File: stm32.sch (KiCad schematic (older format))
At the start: 37 parts, among them J1 USB_B_Micro, J2 Conn_02x05_Odd_Even, U1 STM32F767VITx, U5 LM2937, X1 8MHz

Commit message: Ready To Go! (#53)
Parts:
- C39: Manufacturer (none) -> AVX; VEND (none) -> MOUSER; VEND# (none) -> 581-TAJA156M010R
- D14: Manufacturer DIALIGHT -> (none); Part # 599-0281-007F -> (none); VEND MOUSER -> (none); VEND# 645-599-0281-007F -> (none)
- J1: Manufacturer (none) -> MOLEX; Part # (none) -> 105133-0031; VEND (none) -> MOUSER
- J2: VEND (none) -> MOUSER
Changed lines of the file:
@@
 F 4 "stm32f407_board" H 23450 3775 60  0001 C CNN "PageName"
 F 5 "TAJA156M010RNJ" H 0   0   50  0001 C CNN "Part #"
+F 6 "AVX" H 0   0   50  0001 C CNN "Manufacturer"
+F 7 "MOUSER" H 0   0   50  0001 C CNN "VEND"
+F 8 "581-TAJA156M010R" H 0   0   50  0001 C CNN "VEND#"
 	1    15350 2900
 	1    0    0    -1
@@
 F 3 "" H 12150 3800 60  0001 C CNN
 F 4 "stm32f407_board" H 11525 1275 60  0001 C CNN "PageName"
-F 5 "MOUSER" H -6450 -2300 50  0001 C CNN "VEND"
-F 6 "DIALIGHT" H -6450 -2300 50  0001 C CNN "Manufacturer"
-F 7 "599-0281-007F" H -6450 -2300 50  0001 C CNN "Part #"
-F 8 "645-599-0281-007F" H -6450 -2300 50  0001 C CNN "VEND#"
 	1    12150 3800
 	-1   0    0    1
@@
 F 2 "Connector_PinSocket_2.54mm:PinSocket_2x05_P2.54mm_Vertical_SMD" H 11800 6200 50  0001 C CNN
 F 3 "~" H 11800 6200 50  0001 C CNN
+F 4 "MOUSER" H 0   0   50  0001 C CNN "VEND"
 	1    11800 6200
 	1    0    0    -1
@@
 F 2 "Connector_USB:USB_Micro-B_Molex-105133-0031" H 11650 4150 50  0001 C CNN
 F 3 "~" H 11650 4150 50  0001 C CNN
+F 4 "MOLEX" H 0   0   50  0001 C CNN "Manufacturer"
+F 5 "105133-0031" H 0   0   50  0001 C CNN "Part #"
+F 6 "MOUSER" H 0   0   50  0001 C CNN "VEND"
 	1    11500 4200
 	1    0    0    -1

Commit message: 2x5 BOM and small fix
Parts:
- J2: Manufacturer (none) -> Amphenol; Part # (none) -> 95278-801B10LF; VEND# (none) -> 649-95278-801B10LF
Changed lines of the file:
@@
 F 3 "~" H 11800 6200 50  0001 C CNN
 F 4 "MOUSER" H 0   0   50  0001 C CNN "VEND"
+F 5 "Amphenol" H 0   0   50  0001 C CNN "Manufacturer"
+F 6 "95278-801B10LF" H 0   0   50  0001 C CNN "Part #"
+F 7 "649-95278-801B10LF" H 0   0   50  0001 C CNN "VEND#"
 	1    11800 6200
 	1    0    0    -1

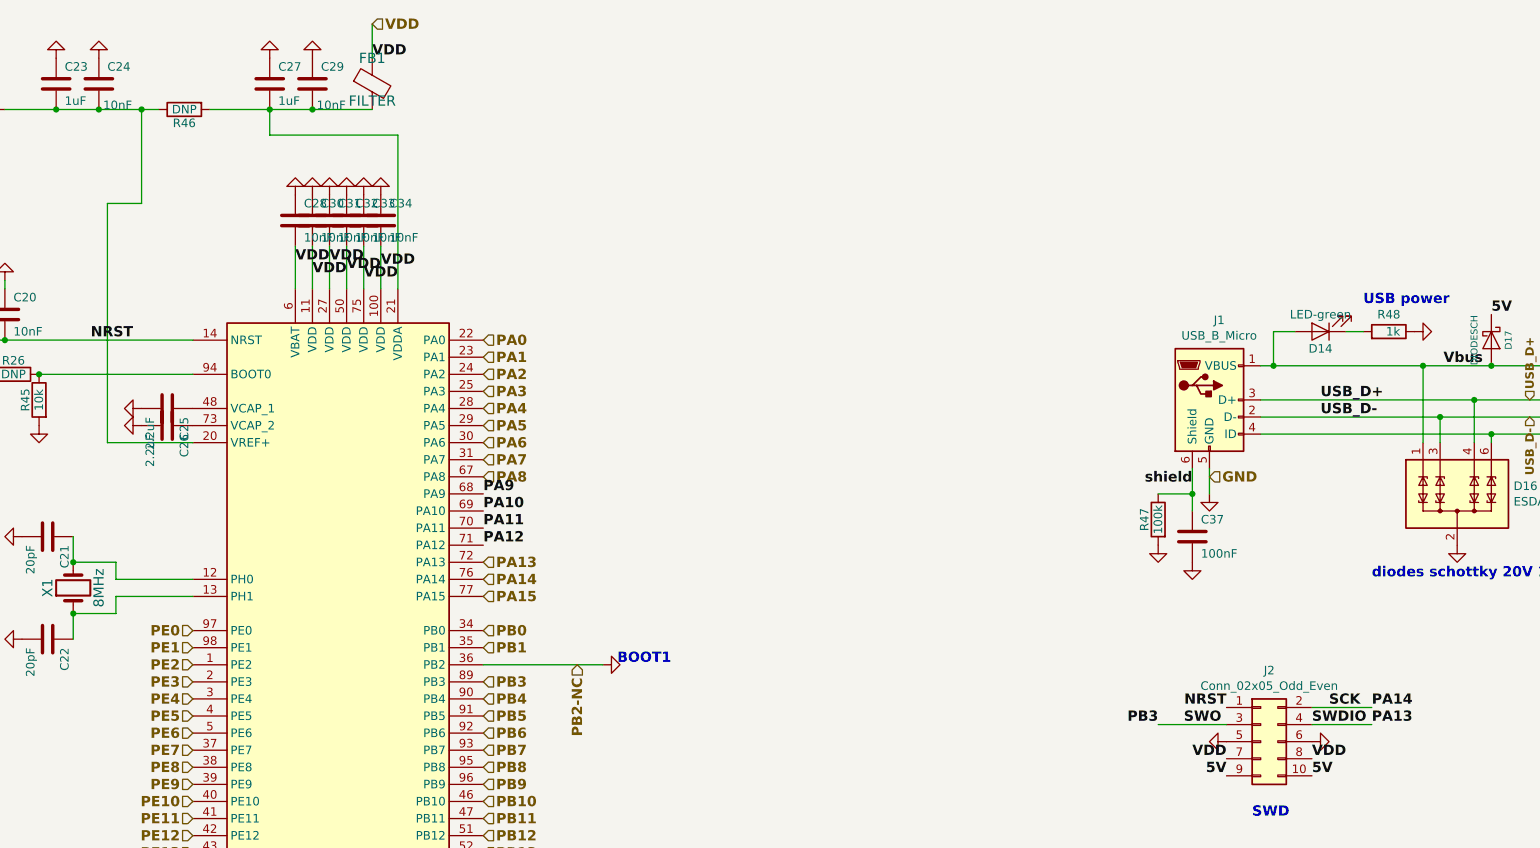
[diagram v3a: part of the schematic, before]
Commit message: from Ola and Jared (#71)
* Update

* removed fp-info-cache from git

* Gerbers

* moved connector

* Mostly Ola's e-mailed copy, plus some of my own fixes to his almost done revision. I also did some house cleaning, with boundary edges, removed most DRC and ERC errors, etc.

* added Fiducial's
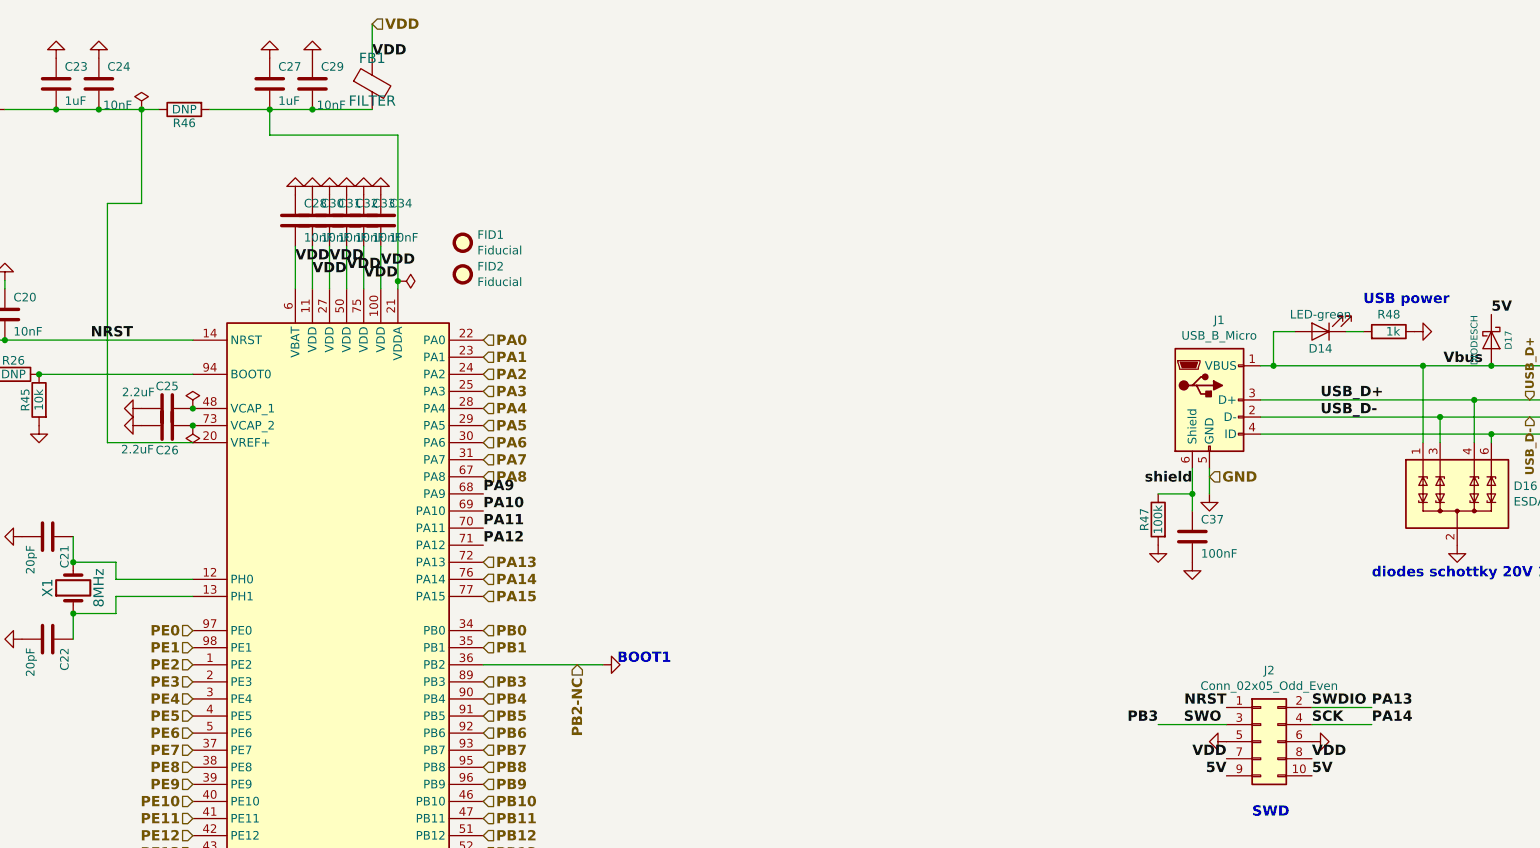
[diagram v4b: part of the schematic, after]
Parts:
- added FID1, FID2: Fiducial, Fiducial:Fiducial_0.5mm_Mask1mm, symbol Mechanical:Fiducial
- C20, C21, C22, C23, C24, C25, C26, C27, C28, C29, C30, C31, C32, C33, C34, C36, C37, C38: footprint Capacitor_SMD:C_0603_1608Metric_Pad1.05x0.95mm_HandSolder -> Capacitor_SMD:C_0603_1608Metric
- C39: footprint Capacitor_SMD:C_1206_3216Metric_Pad1.42x1.75mm_HandSolder -> Capacitor_SMD:C_1206_3216Metric
- D17: footprint Capacitor_SMD:C_0603_1608Metric_Pad1.05x0.95mm_HandSolder -> Diode_SMD:D_0603_1608Metric
- D19: footprint LED_SMD:LED_0603_1608Metric_Pad1.05x0.95mm_HandSolder -> LED_SMD:LED_0603_1608Metric
- R26, R43, R44, R45, R46, R47, R48, R50: footprint Resistor_SMD:R_0603_1608Metric_Pad1.05x0.95mm_HandSolder -> Resistor_SMD:R_0603_1608Metric
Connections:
- net PA13: now also J2.2 (Pin_2); no longer J2.4 (Pin_4)
- net PA14: now also J2.4 (Pin_4); no longer J2.2 (Pin_2)

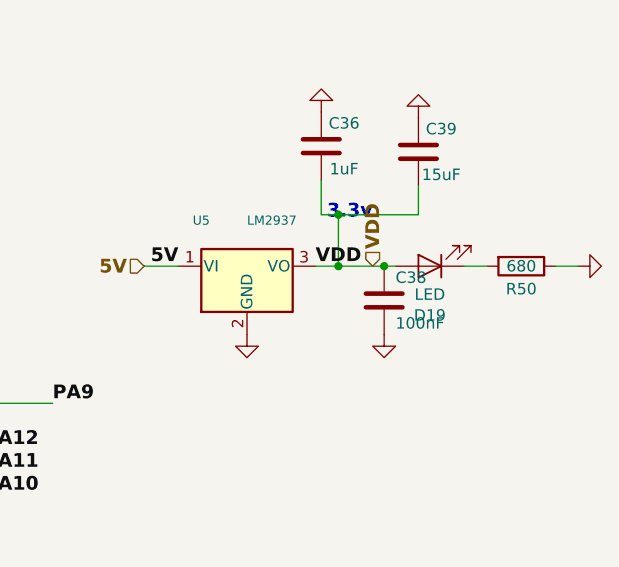
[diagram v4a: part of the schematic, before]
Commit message: Updated logo symbol and footprint, BOM is 99% entered in KC schematic now.
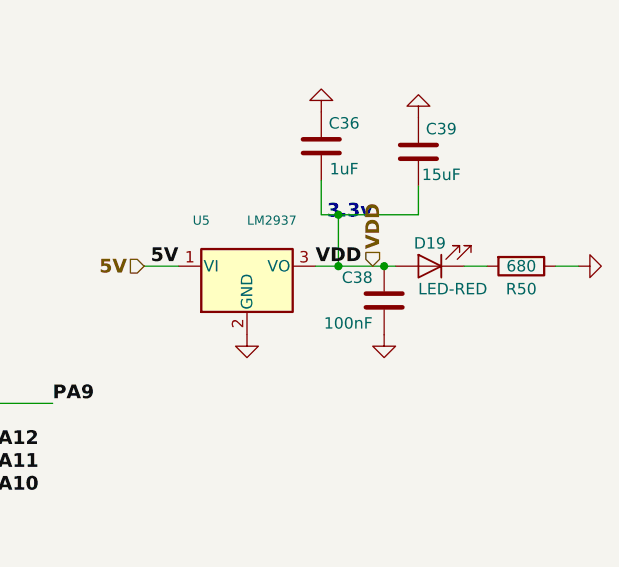
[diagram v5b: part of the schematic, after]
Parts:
- C20, C24, C28, C29, C30, C31, C32, C33, C34: Manufacturer (none) -> KEMET; Part # (none) -> C0603C103K1RACTU; VEND (none) -> DIGI; VEND# (none) -> 399-3189-1-ND
- C21, C22: Manufacturer (none) -> AVX; Part # (none) -> 06035A200FAT2A; VEND (none) -> DIGI; VEND# (none) -> 478-10299-1-ND
- C23, C27, C36: Manufacturer (none) -> Taiyo Yuden; PageName stm32f407_board -> (none); Part # (none) -> UMK107BJ105KA-T; VEND (none) -> DIGI; VEND# (none) -> 587-2400-1-ND
- C25, C26: Manufacturer (none) -> MURATA; Part # (none) -> GRM188R6YA225KA12D; VEND (none) -> DIGI; VEND# (none) -> 490-7204-1-ND
- C37, C38: Manufacturer (none) -> KEMET; Part # (none) -> C0603C104J5RACTU; VEND (none) -> DIGI; VEND# (none) -> 399-7844-1-ND
- C39: VEND MOUSER -> DIGI; VEND# 581-TAJA156M010R -> 478-1661-1-ND
- D14: Manufacturer (none) -> DiaLight; Part # (none) -> 5990281007F; VEND (none) -> DIGI; VEND# (none) -> 350-4365-1-ND
- D16: Manufacturer (none) -> ST; Part # (none) -> ESDA6V1BC6; VEND (none) -> DIGI; VEND# (none) -> 497-6635-1-ND
- D17: Manufacturer (none) -> ST; Part # ST,BAT60JFILM -> BAT60JFILM; VEND (none) -> DIGI; VEND# DIGI,497-3707-1-ND -> 497-3707-1-ND
- D19: value LED -> LED-RED; Manufacturer (none) -> Lite-On; Part # (none) -> LTST-S270KRKT; VEND (none) -> DIGI; VEND# (none) -> 160-1479-1-ND
- FB1: Manufacturer (none) -> Murata; VEND MOUSER -> DIGI; VEND# 81-BLM21P221SG -> 490-1054-1-ND
- FID1, FID2: Manufacturer (none) -> DNP; Part # (none) -> DNP; VEND (none) -> DNP; VEND# (none) -> DNP
- J1: VEND# (none) -> 538-105133-0031
- R26, R46: Manufacturer (none) -> DNP; Part # (none) -> DNP; VEND (none) -> DIGI; VEND# (none) -> DNP
- R43, R45: Manufacturer (none) -> StackPole; Part # (none) -> RMCF0603JT10K0; VEND (none) -> DIGI; VEND# (none) -> RMCF0603JT10K0CT-ND
- R44: Manufacturer (none) -> StackPole; Part # (none) -> RMCF0603ZT0R00; VEND (none) -> DIGI; VEND# (none) -> RMCF0603ZT0R00CT-ND
- R47: Manufacturer (none) -> StackPole; Part # (none) -> RMCF0603JT100K; VEND MOUSER -> DIGI; VEND# (none) -> RMCF0603JT100KCT-ND
- R48: Manufacturer (none) -> StackPole; Part # (none) -> RMCF0603JJ1K00; VEND (none) -> DIGI; VEND# (none) -> RMCF0603JJ1K00CT-ND
- R50: Manufacturer (none) -> StackPole; Part # (none) -> RMCF0603FT680R; VEND (none) -> DIGI; VEND# (none) -> RMCF0603FT680RCT-ND
- U1: Manufacturer (none) -> ST; Part # 511-STM32F767VIT6 -> STM32F767VIT6; VEND (none) -> DIGI; VEND# 511-STM32F767VIT6 -> 497-16643-ND
- U5: Manufacturer (none) -> TI; Part # 926-LM2937IMP3.3NOPB -> LM2937IMP-3.3/NOPB; VEND MOUSER -> DIGI; VEND# (none) -> LM2937IMP-3.3/NOPBCT-ND
- X1: Manufacturer (none) -> NDK; VEND MOUSER -> DIGI; VEND# 344-NX3225GD8MCRA3 -> 644-1178-1-ND

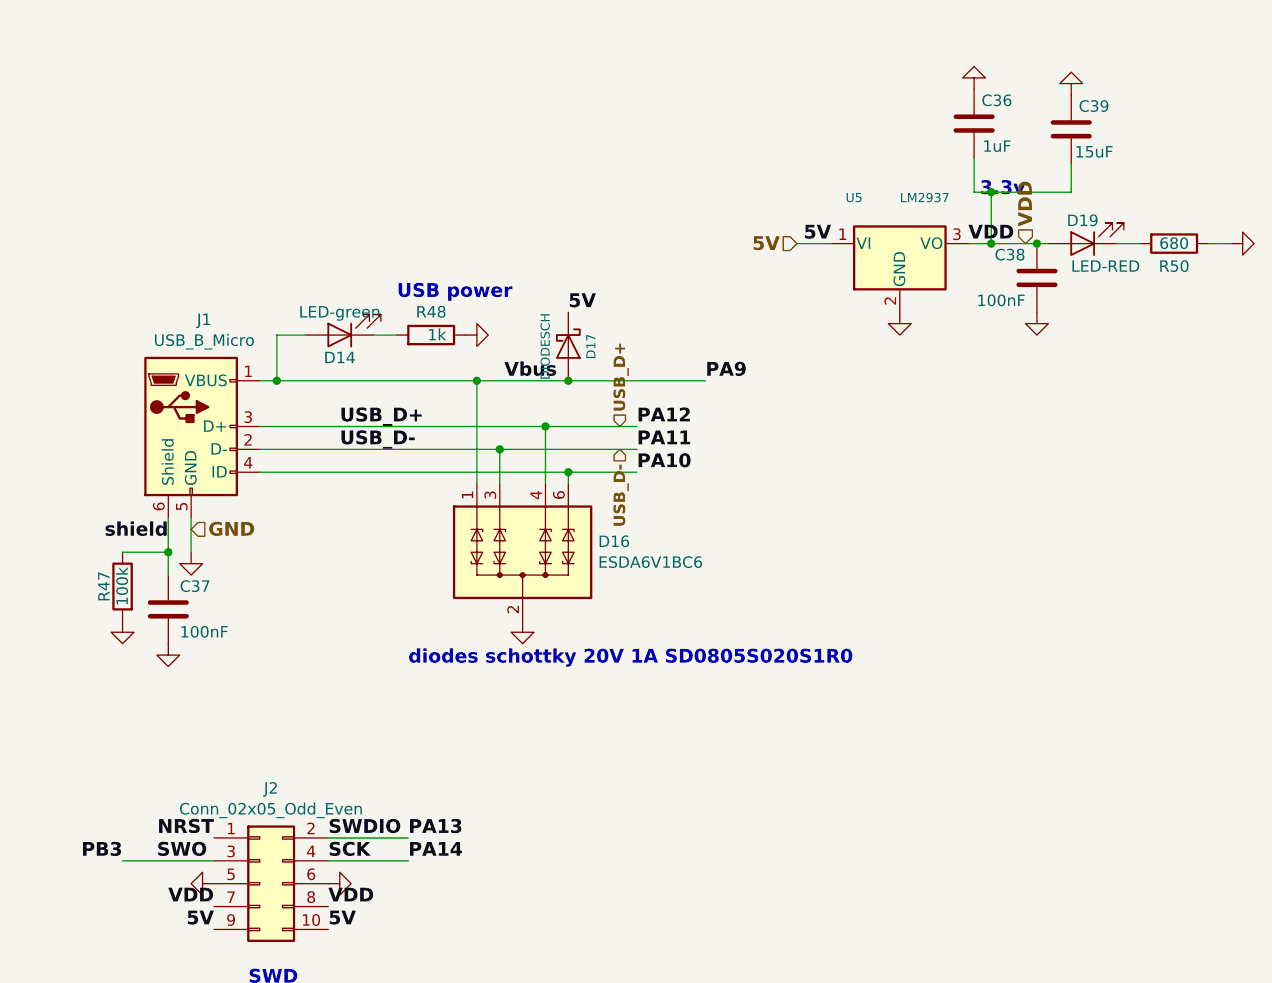
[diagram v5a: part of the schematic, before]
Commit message: Some general MISC cleanup of overlapping text, etc.
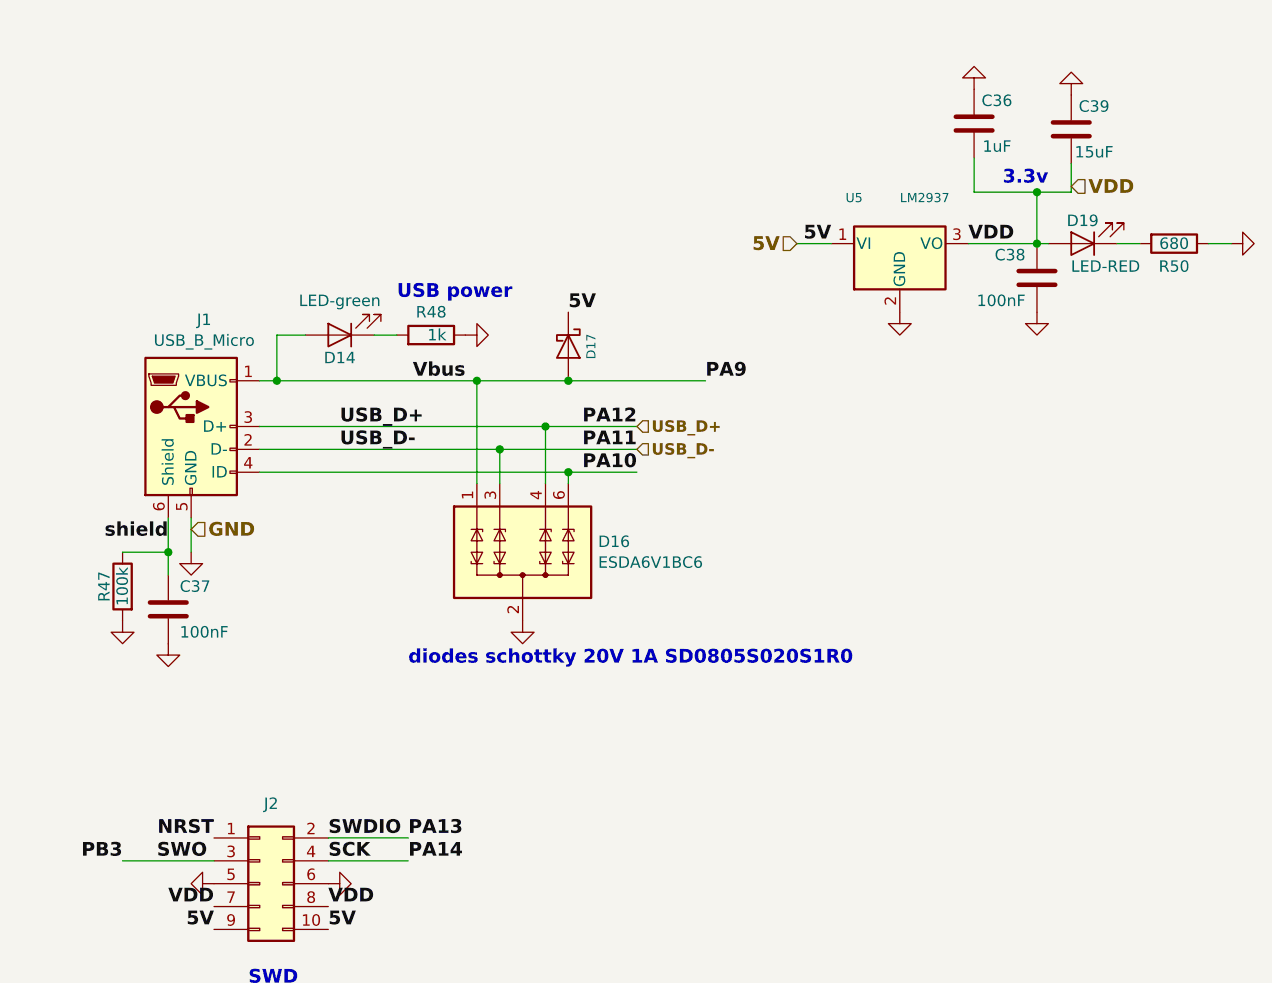
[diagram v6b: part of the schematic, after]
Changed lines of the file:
@@
 P 13150 3850
 F 0 "D17" H 13150 3950 40  0000 C CNN
-F 1 "DIODESCH" H 13150 3750 40  0000 C CNN
+F 1 "DIODESCH" H 13150 3750 40  0001 C CNN
 F 2 "Diode_SMD:D_0603_1608Metric" V 1405 1550 60  0001 C CNN
 F 3 "" H 13150 3850 60  0001 C CNN
@@
 P 12150 3800
 F 0 "D14" H 12150 3900 50  0000 C CNN
-F 1 "LED-green" H 12150 3700 50  0000 C CNN
+F 1 "LED-green" H 12150 3650 50  0000 C CNN
 F 2 "Capacitor_SMD:C_0603_1608Metric_Pad1.05x0.95mm_HandSolder" V 5   1700 60  0001 C CNN
 F 3 "" H 12150 3800 60  0001 C CNN
@@
 	-1   0    0    1
 $EndComp
-Text Notes 14950 3200 0    60   ~ 12
+Text Notes 15050 3150 0    60   ~ 12
 3.3v
-Text Label 13100 4000 2    60   ~ 12
+Text Label 12700 4000 2    60   ~ 12
 Vbus
 Text Notes 12450 5250 0    60   ~ 12
 diodes schottky 20V 1A SD0805S020S1R0
-Text Label 13450 4400 0    60   ~ 12
+Text Label 13450 4400 2    60   ~ 12
 PA10
 Text Label 13750 4000 0    60   ~ 12
@@
 	12300 3800 12400 3800
 Wire Wire Line
-	14900 3400 15000 3400
+	14900 3400 15200 3400
 $Comp
 L Device:LED D?
@@
 	0    -1   -1   0
 $EndComp
-Text HLabel 15150 3400 1    60   Input ~ 12
+Text HLabel 15350 3150 2    60   Input ~ 12
 VDD
 $Comp
@@
 	1    0    0    -1
 $EndComp
-Text Label 13450 4300 0    60   ~ 12
+Text Label 13450 4300 2    60   ~ 12
 PA11
-Text Label 13450 4200 0    60   ~ 12
+Text Label 13450 4200 2    60   ~ 12
 PA12
 Wire Wire Line
@@
 U 1 1 5CDE2131
 P 11800 6200
-F 0 "J2" H 11850 6617 50  0000 C CNN
-F 1 "Conn_02x05_Odd_Even" H 11850 6526 50  0000 C CNN
+F 0 "J2" H 11850 6550 50  0000 C CNN
+F 1 "Conn_02x05_Odd_Even" H 11850 6526 50  0001 C CNN
 F 2 "Connector_PinSocket_2.54mm:PinSocket_2x05_P2.54mm_Vertical_SMD" H 11800 6200 50  0001 C CNN
 F 3 "~" H 11800 6200 50  0001 C CNN
@@
 NoConn ~ 7250 8650
 NoConn ~ 7250 8750
-Text HLabel 13375 4200 1    50   Input ~ 10
+Text HLabel 13450 4200 2    50   Input ~ 10
 USB_D+
-Text HLabel 13375 4300 3    50   Input ~ 10
+Text HLabel 13450 4300 2    50   Input ~ 10
 USB_D-
-$Comp
-L Device:C C36
-U 1 1 5D073BF7
-P 14925 2875
-F 0 "C36" H 15025 2975 50  0000 C CNN
-F 1 "1uF" H 15025 2775 50  0000 C CNN
-F 2 "Capacitor_SMD:C_0603_1608Metric" V 11505 4175 60  0001 C CNN
-F 3 "" H 14925 2875 60  0001 C CNN
-F 4 "UMK107BJ105KA-T" H 0   0   50  0001 C CNN "Part #"
-F 5 "DIGI" H 0   0   50  0001 C CNN "VEND"
-F 6 "587-2400-1-ND" H 0   0   50  0001 C CNN "VEND#"
-F 7 "Taiyo Yuden" H 0   0   50  0001 C CNN "Manufacturer"
-	1    14925 2875
-	1    0    0    -1
-$EndComp
-$Comp
-L power:GND #PWR0133
-U 1 1 5D07522E
-P 14925 2725
-F 0 "#PWR0133" H 14925 2725 30  0001 C CNN
-F 1 "GND" H 14925 2655 30  0001 C CNN
-F 2 "" H 14925 2725 60  0000 C CNN
-F 3 "" H 14925 2725 60  0000 C CNN
-	1    14925 2725
-	-1   0    0    1
-$EndComp
-Wire Wire Line
-	14925 3025 14925 3175
-Wire Wire Line
-	14925 3175 15000 3175
-Wire Wire Line
-	15000 3175 15000 3400
-Connection ~ 15000 3400
-Wire Wire Line
-	15000 3400 15200 3400
+Wire Wire Line
+	14925 3175 15200 3175
+Wire Wire Line
+	15200 3175 15200 3400
 Wire Wire Line
 	15350 3050 15350 3175
 Wire Wire Line
-	15350 3175 15000 3175
-Connection ~ 15000 3175
+	15350 3175 15200 3175
+Connection ~ 15200 3175
 $Comp
 L Device:R R26
@@
 	1    0    0    -1
 $EndComp
+Wire Wire Line
+	14925 3025 14925 3175
+$Comp
+L power:GND #PWR0133
+U 1 1 5D07522E
+P 14925 2725
+F 0 "#PWR0133" H 14925 2725 30  0001 C CNN
+F 1 "GND" H 14925 2655 30  0001 C CNN
+F 2 "" H 14925 2725 60  0000 C CNN
+F 3 "" H 14925 2725 60  0000 C CNN
+	1    14925 2725
+	-1   0    0    1
+$EndComp
+$Comp
+L Device:C C36
+U 1 1 5D073BF7
+P 14925 2875
+F 0 "C36" H 15025 2975 50  0000 C CNN
+F 1 "1uF" H 15025 2775 50  0000 C CNN
+F 2 "Capacitor_SMD:C_0603_1608Metric" V 11505 4175 60  0001 C CNN
+F 3 "" H 14925 2875 60  0001 C CNN
+F 4 "UMK107BJ105KA-T" H 0   0   50  0001 C CNN "Part #"
+F 5 "DIGI" H 0   0   50  0001 C CNN "VEND"
+F 6 "587-2400-1-ND" H 0   0   50  0001 C CNN "VEND#"
+F 7 "Taiyo Yuden" H 0   0   50  0001 C CNN "Manufacturer"
+	1    14925 2875
+	1    0    0    -1
+$EndComp
